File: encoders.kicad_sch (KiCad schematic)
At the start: 3 parts, among them J401 Encoder Commector, J402 External encoders power

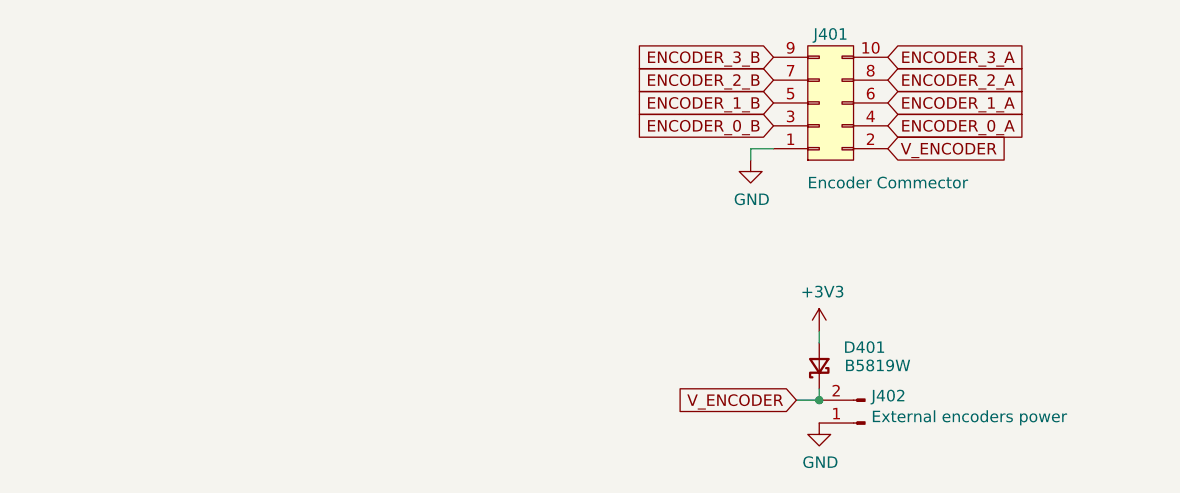
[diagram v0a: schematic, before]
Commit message: Add USB sensing and power management components to the schematic
- Introduced a junction for USB sensing at coordinates (173.99, 64.77).
- Added multiple wires connecting various components to the new junction.
- Created a global label "USB_SENSE" for the USB sensing functionality.
- Updated references for power components to a new numbering scheme (#PWR0501 to #PWR0509).
- Added resistors R505 and R506 with specified values and footprints.
- Included power symbols for +5V and GND with appropriate references and properties.
- Ensured all new components are included in the BOM and marked for simulation.
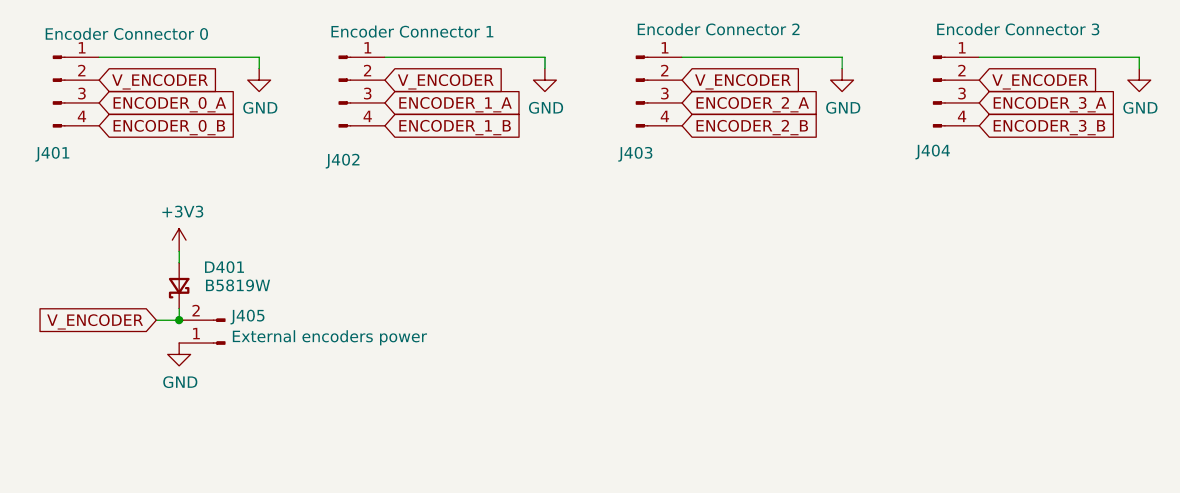
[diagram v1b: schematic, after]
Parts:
- removed J401: Encoder Commector, VsReality_Footprints:Encoder_PinHeader_4x04_P2.54mm_Vertical, symbol smart_motor_controller-rescue:EncoderPinHeaderConnector_04-VsReality_Symbols
- added J401: Encoder Connector 0, Connector_JST:JST_PH_B4B-PH-K_1x04_P2.00mm_Vertical, symbol Connector:Conn_01x04_Pin
- added J402: Encoder Connector 1, Connector_JST:JST_PH_B4B-PH-K_1x04_P2.00mm_Vertical, symbol Connector:Conn_01x04_Pin
- added J403: Encoder Connector 2, Connector_JST:JST_PH_B4B-PH-K_1x04_P2.00mm_Vertical, symbol Connector:Conn_01x04_Pin
- added J404: Encoder Connector 3, Connector_JST:JST_PH_B4B-PH-K_1x04_P2.00mm_Vertical, symbol Connector:Conn_01x04_Pin
- renumbered J402 to J405
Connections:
- net ENCODER_0_A: now also J401.3 (Pin_3)
- net ENCODER_0_B: now also J401.4 (Pin_4)
- net ENCODER_1_A: now also J402.3 (Pin_3)
- net ENCODER_1_B: now also J402.4 (Pin_4)
- net ENCODER_2_A: now also J403.3 (Pin_3)
- net ENCODER_2_B: now also J403.4 (Pin_4)
- net ENCODER_3_A: now also J404.3 (Pin_3)
- net ENCODER_3_B: now also J404.4 (Pin_4)
- net GND: now also J401.1 (Pin_1), J402.1 (Pin_1), J403.1 (Pin_1), J404.1 (Pin_1)
- net V_ENCODER: now also J401.2 (Pin_2), J402.2 (Pin_2), J403.2 (Pin_2), J404.2 (Pin_2)
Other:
- moved on the sheet: D401, J405
